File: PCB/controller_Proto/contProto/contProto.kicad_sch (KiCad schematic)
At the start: 85 parts, among them J1 Conn_01x05, J10 JST_1mm_3, J11 JST_1mm_3, J12 JST_1mm_3, J13 Conn_01x02_Socket, J14 Conn_01x02_Socket, J15 Conn_01x04, J16 Conn_01x04, J17 Conn_01x10_Pin, J18 JST_1mm_3, J19 Conn_01x08_Socket, J2 Conn_01x04, J20 JST_1mm_3, J21 JST_1mm_3, J22 JST_1mm_3, J23 JST_1mm_3, J24 Conn_01x03_Socket, J25 Conn_01x03_Socket, J26 Conn_01x03_Socket, J27 Conn_01x03_Socket, J28 Conn_01x12_Socket, J29 Conn_01x12_Socket, J3 Conn_01x10_Pin, J30 Conn_01x12_Socket, J31 Conn_01x12_Socket, J32 Conn_01x02_Socket, J33 Conn_01x02_Socket, J34 Conn_01x02_Socket, J35 Conn_01x02_Socket, J36 Conn_01x05, J37 Conn_01x05, J4 JST_1mm_3, J5 Conn_01x05, J6 JST_1mm_3, J7 Conn_01x05, J8 Conn_01x05, J9 Conn_01x04, SW1 SMD_12x12mm_h8.5mm, SW10 SMD_12x12mm_h8.5mm, SW11 SMD_12x12mm_h8.5mm, SW12 SMD_12x12mm_h8.5mm, SW13 SMD_12x12mm_h8.5mm, SW14 SMD_12x12mm_h8.5mm, SW15 SMD_12x12mm_h8.5mm, SW16 SMD_12x12mm_h8.5mm, SW17 SMD_12x12mm_h8.5mm, SW18 SMD_12x12mm_h8.5mm, SW19 SMD_12x12mm_h8.5mm, SW2 SMD_12x12mm_h8.5mm, SW20 SMD_12x12mm_h8.5mm, SW3 SMD_12x12mm_h8.5mm, SW4 SMD_12x12mm_h8.5mm, SW5 SMD_12x12mm_h8.5mm, SW6 SMD_12x12mm_h8.5mm, SW7 SMD_12x12mm_h8.5mm, SW8 SMD_12x12mm_h8.5mm, SW9 SMD_12x12mm_h8.5mm, U1 ProMicroC, U2 ProMicroC, U3 DRV5033FAxLPG, U4 DRV5033FAxLPG

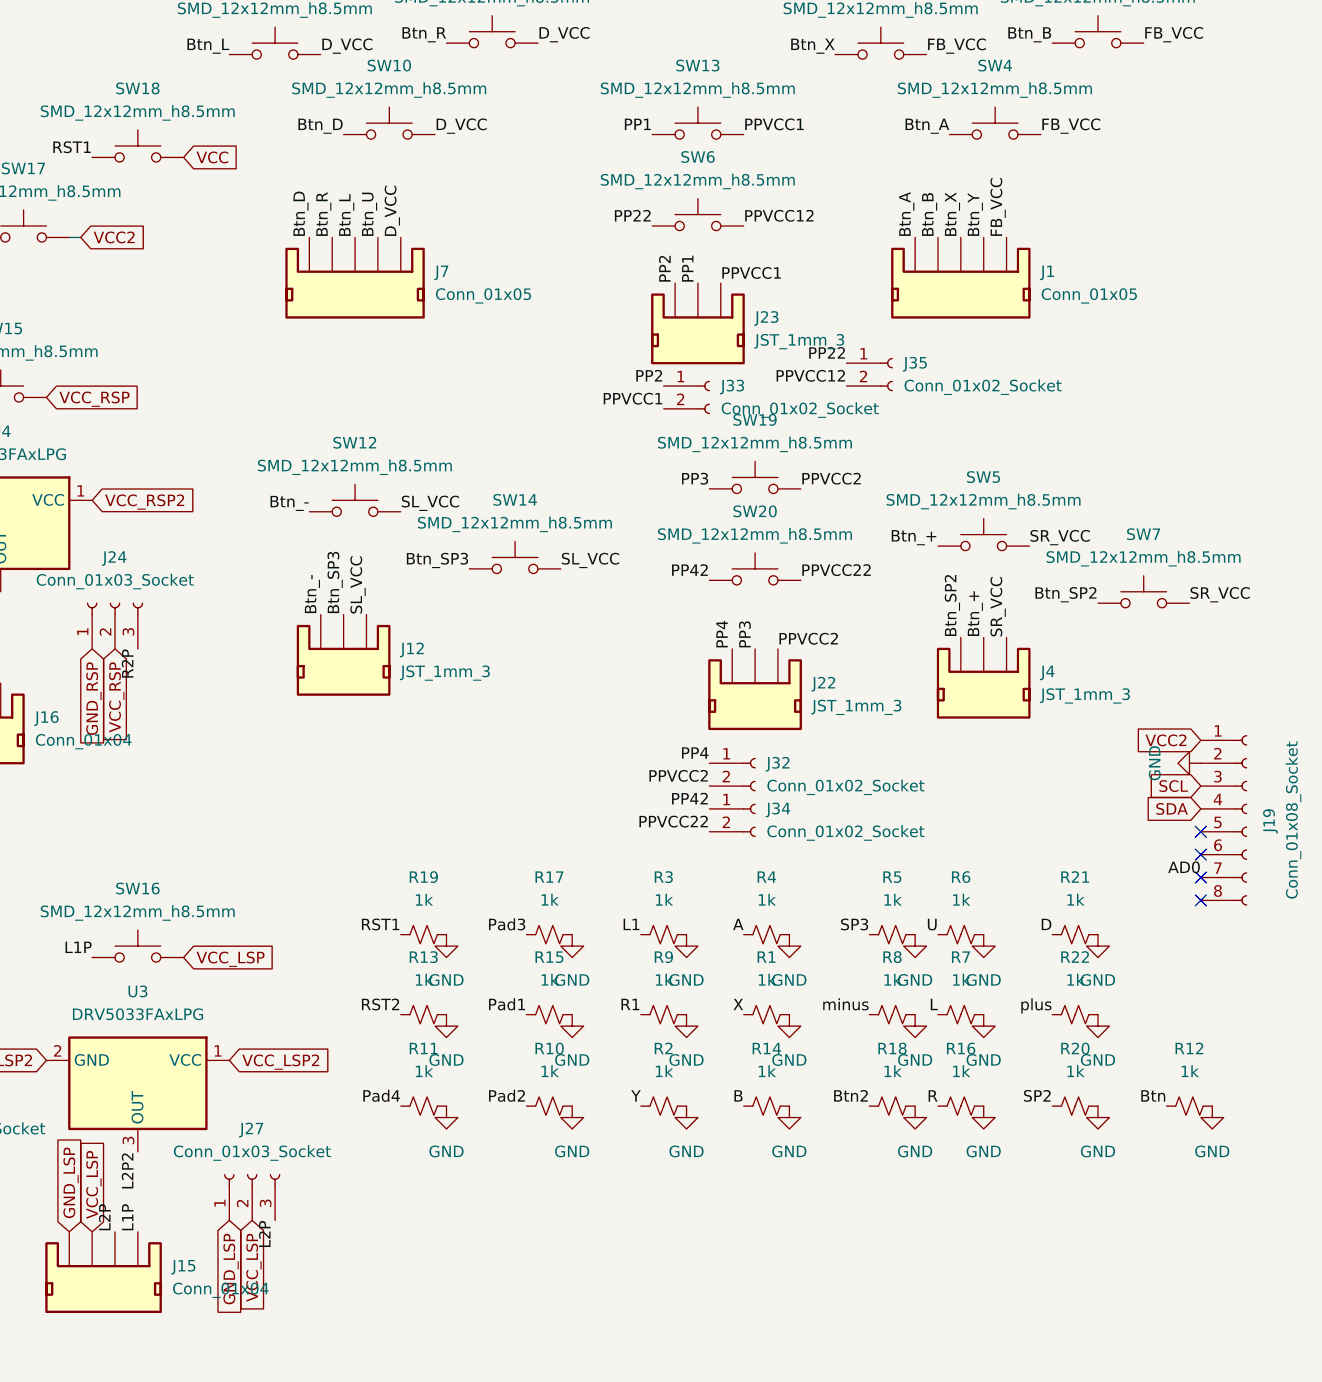
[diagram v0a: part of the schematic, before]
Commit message: move res big v
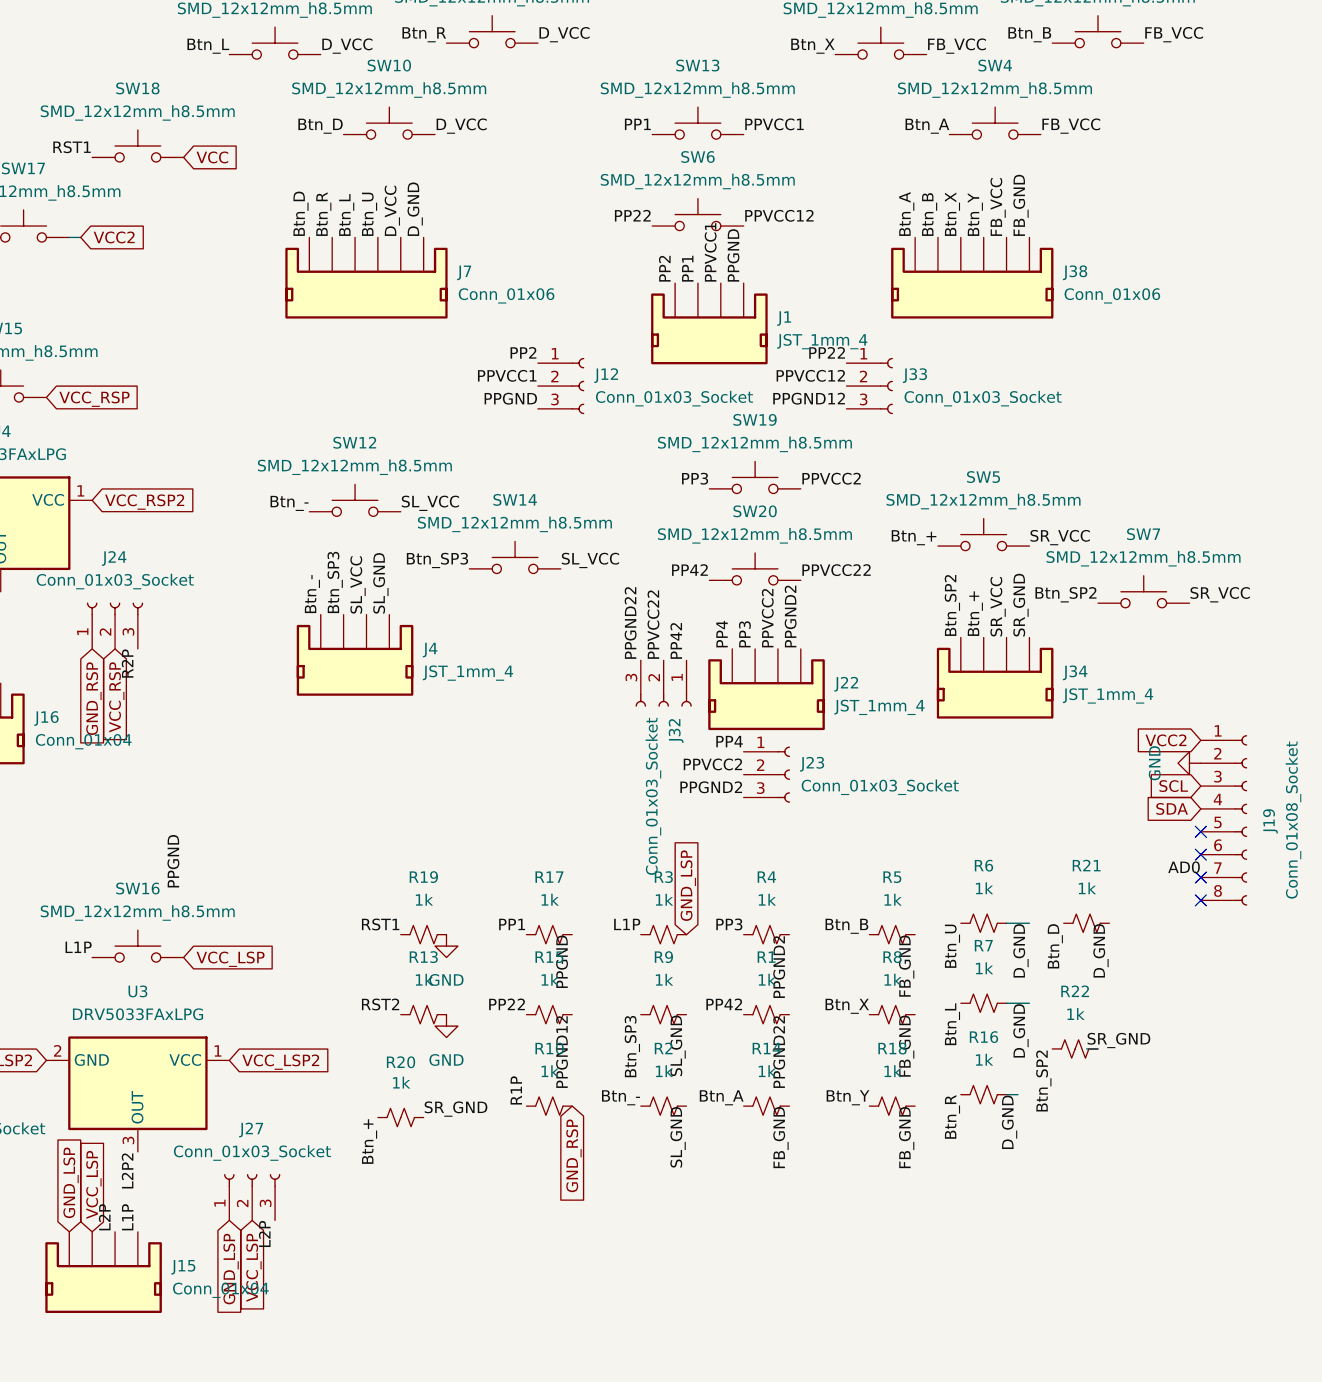
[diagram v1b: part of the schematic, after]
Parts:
- removed J1, J7: Conn_01x05, Connector_JST:JST_GH_BM05B-GHS-TBT_1x05-1MP_P1.25mm_Vertical, symbol PCM_SparkFun-Connector:Conn_01x05_JST_P1.0mm_Horizontal_SMD
- removed J12, J22, J23, J4: JST_1mm_3, Connector_JST:JST_GH_BM03B-GHS-TBT_1x03-1MP_P1.25mm_Vertical, symbol PCM_SparkFun-Connector:Conn_01x03_JST_P1.0mm_Horizontal_SMD
- removed J32, J33, J34, J35: Conn_01x02_Socket, Connector_PinSocket_2.54mm:PinSocket_1x02_P2.54mm_Vertical, symbol Connector:Conn_01x02_Socket
- removed R11, R12: 1k, PCM_SparkFun-Resistor:R_0402_1005Metric, symbol PCM_SparkFun-Resistor:1k_0402
- added J1, J22, J34, J4: JST_1mm_4, PCM_SparkFun-Connector:JST_1x04_P1.0mm_Horizontal_SMD, symbol PCM_SparkFun-Connector:Conn_01x04_JST_P1.0mm_Horizontal_SMD
- added J12, J23, J32, J33: Conn_01x03_Socket, Connector_PinSocket_2.54mm:PinSocket_1x03_P2.54mm_Vertical, symbol Connector:Conn_01x03_Socket
- added J38, J7: Conn_01x06, PCM_SparkFun-Connector:JST_1x06_P1.0mm_Horizontal_SMD, symbol PCM_SparkFun-Connector:Conn_01x06_JST_P1.0mm_Horizontal_SMD
- J13, J14: footprint Connector_PinSocket_1.00mm:PinSocket_1x02_P1.00mm_Vertical -> Connector_PinSocket_2.54mm:PinSocket_1x02_P2.54mm_Vertical
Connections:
- net A: no longer R4.1
- net B: no longer R14.1
- net Btn2: no longer R18.1
- net Btn_+: now also R20.1, J34.3
- net Btn_-: now also R2.1, J4.4
- net Btn_A: now also R14.1, J38.6
- net Btn_B: now also R5.1, J38.5
- net Btn_D: now also R21.1, J7.6
- net Btn_L: now also R7.1, J7.4
- net Btn_R: now also R16.1, J7.5
- net Btn_SP2: now also R22.1, J34.4
- net Btn_SP3: now also R9.1, J4.3
- net Btn_U: now also R6.1, J7.3
- net Btn_X: now also R8.1, J38.4
- net Btn_Y: now also R18.1, J38.3
- net D: no longer R21.1
- net D_VCC: now also J7.2
- net FB_VCC: now also J38.2
- net GND: no longer R1.2, R10.2, R14.2, R15.2, R16.2, R17.2, R18.2, R2.2, R20.2, R21.2, R22.2, R3.2, R4.2, R5.2, R6.2, R7.2, R8.2, R9.2
- net GND_LSP: now also R3.2
- net GND_RSP: now also R10.2
- net L: no longer R7.1
- net L1: no longer R3.1
- net L1P: now also R3.1
- net PP1: now also R17.1, J1.3
- net PP2: now also J1.4, J12.1 (Pin_1)
- net PP22: now also R15.1, J33.1 (Pin_1)
- net PP3: now also R4.1, J22.3
- net PP4: now also J22.4, J23.1 (Pin_1)
- net PP42: now also R1.1, J32.1 (Pin_1)
- net PPVCC1: now also J1.2, J12.2 (Pin_2)
- net PPVCC12: now also J33.2 (Pin_2)
- net PPVCC2: now also J22.2, J23.2 (Pin_2)
- net PPVCC22: now also J32.2 (Pin_2)
- net Pad1: no longer R15.1
- net Pad2: no longer R10.1
- net Pad3: no longer R17.1
- net R: no longer R16.1
- net R1: no longer R9.1
- net R1P: now also R10.1
- net SL_VCC: now also J4.2
- net SP2: no longer R20.1
- net SP3: no longer R5.1
- net SR_VCC: now also J34.2
- net U: no longer R6.1
- net X: no longer R1.1
- net Y: no longer R2.1
- net minus: no longer R8.1
- net plus: no longer R22.1
- new net D_GND: J7.1, R16.2, R21.2, R6.2, R7.2
- new net FB_GND: J38.1, R14.2, R18.2, R5.2, R8.2
- new net PPGND: J1.1, J12.3 (Pin_3), R17.2
- new net PPGND12: J33.3 (Pin_3), R15.2
- new net PPGND2: J22.1, J23.3 (Pin_3), R4.2
- new net PPGND22: J32.3 (Pin_3), R1.2
- new net SL_GND: J4.1, R2.2, R9.2
- new net SR_GND: J34.1, R20.2, R22.2
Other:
- moved on the sheet: R16, R20, R21, R22, R6, R7
